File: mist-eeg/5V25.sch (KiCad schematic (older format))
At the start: 14 parts, among them U5 TPS63070

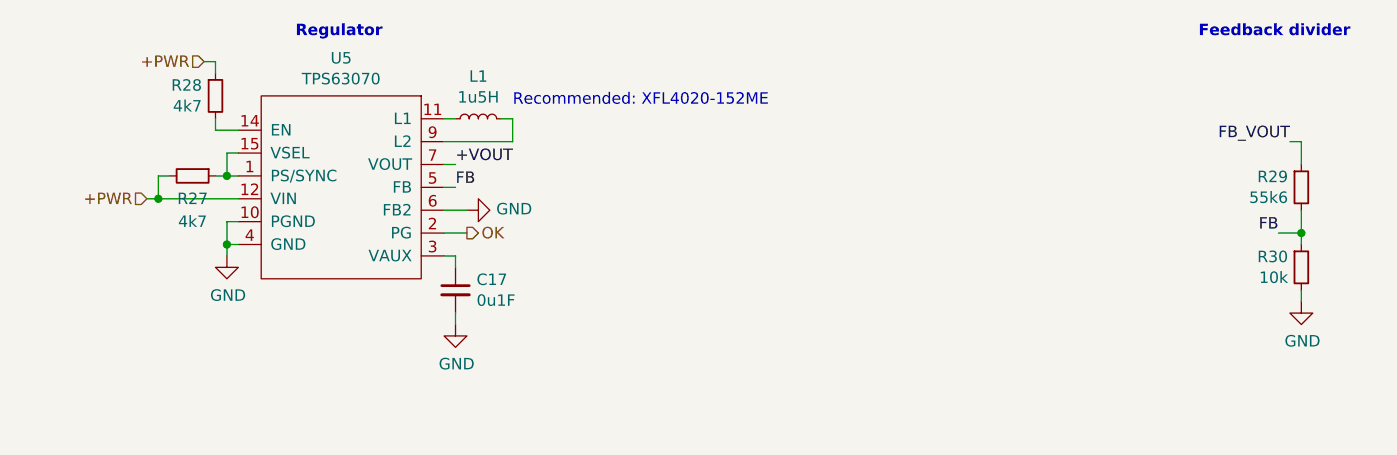
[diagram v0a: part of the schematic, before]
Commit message: Finish schematic and create interface specifications
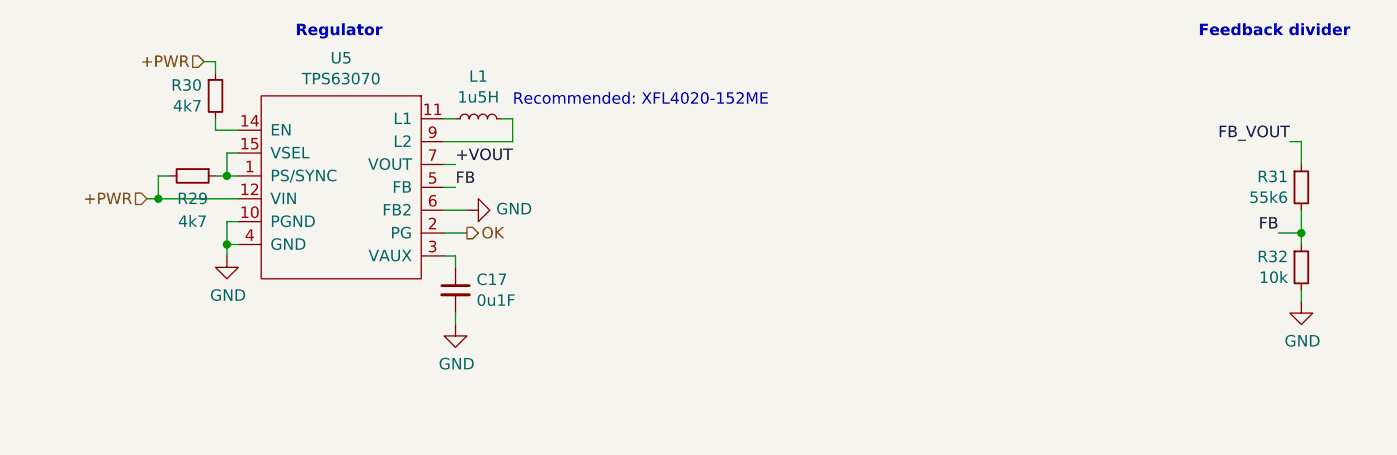
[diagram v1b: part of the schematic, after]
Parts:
- renumbered R27 to R29, R28 to R30, R29 to R31, R30 to R32
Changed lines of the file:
@@
 	3950 2450 4000 2450
 $Comp
-L Device:R_Small R27
+L Device:R_Small R29
 U 1 1 60DC4DE3
 P 3800 2550
-F 0 "R27" V 3900 2550 50  0000 C CNN
+F 0 "R29" V 3900 2550 50  0000 C CNN
 F 1 "4k7" V 4000 2550 50  0000 C CNN
 F 2 "Resistor_SMD:R_0201_0603Metric" H 3800 2550 50  0001 C CNN
@@
 Connection ~ 6250 4500
 $Comp
-L Device:R_Small R29
+L Device:R_Small R31
 U 1 1 60DEB0F2
 P 8650 2600
-F 0 "R29" H 8592 2646 50  0000 R CNN
+F 0 "R31" H 8592 2646 50  0000 R CNN
 F 1 "55k6" H 8592 2555 50  0000 R CNN
 F 2 "Resistor_SMD:R_0603_1608Metric" H 8650 2600 50  0001 C CNN
@@
 $EndComp
 $Comp
-L Device:R_Small R30
+L Device:R_Small R32
 U 1 1 60DEB255
 P 8650 2950
-F 0 "R30" H 8592 2996 50  0000 R CNN
+F 0 "R32" H 8592 2996 50  0000 R CNN
 F 1 "10k" H 8592 2905 50  0000 R CNN
 F 2 "Resistor_SMD:R_0603_1608Metric" H 8650 2950 50  0001 C CNN
@@
 Regulator
 $Comp
-L Device:R_Small R28
+L Device:R_Small R30
 U 1 1 60EEA7D5
 P 3900 2200
-F 0 "R28" H 3841 2246 50  0000 R CNN
+F 0 "R30" H 3841 2246 50  0000 R CNN
 F 1 "4k7" H 3841 2155 50  0000 R CNN
 F 2 "Resistor_SMD:R_0201_0603Metric" H 3900 2200 50  0001 C CNN
@@
 Recommended: XFL4020-152ME
 $Comp
-L power:GND #PWR035
+L power:GND #PWR036
 U 1 1 610AC588
 P 2450 4950
-F 0 "#PWR035" H 2450 4700 50  0001 C CNN
+F 0 "#PWR036" H 2450 4700 50  0001 C CNN
 F 1 "GND" V 2455 4822 50  0000 R CNN
 F 2 "" H 2450 4950 50  0001 C CNN
@@
 $EndComp
 $Comp
-L power:GND #PWR039
+L power:GND #PWR040
 U 1 1 610AC95F
 P 6250 5050
-F 0 "#PWR039" H 6250 4800 50  0001 C CNN
+F 0 "#PWR040" H 6250 4800 50  0001 C CNN
 F 1 "GND" H 6255 4877 50  0000 C CNN
 F 2 "" H 6250 5050 50  0001 C CNN
@@
 $EndComp
 $Comp
-L power:GND #PWR036
+L power:GND #PWR037
 U 1 1 610ACD33
 P 3950 2900
-F 0 "#PWR036" H 3950 2650 50  0001 C CNN
+F 0 "#PWR037" H 3950 2650 50  0001 C CNN
 F 1 "GND" H 3955 2727 50  0000 C CNN
 F 2 "" H 3950 2900 50  0001 C CNN
@@
 $EndComp
 $Comp
-L power:GND #PWR037
+L power:GND #PWR038
 U 1 1 610AD0E9
 P 4950 3200
-F 0 "#PWR037" H 4950 2950 50  0001 C CNN
+F 0 "#PWR038" H 4950 2950 50  0001 C CNN
 F 1 "GND" H 4955 3027 50  0000 C CNN
 F 2 "" H 4950 3200 50  0001 C CNN
@@
 $EndComp
 $Comp
-L power:GND #PWR038
+L power:GND #PWR039
 U 1 1 610AD47F
 P 5000 2700
-F 0 "#PWR038" H 5000 2450 50  0001 C CNN
+F 0 "#PWR039" H 5000 2450 50  0001 C CNN
 F 1 "GND" V 5005 2572 50  0000 R CNN
 F 2 "" H 5000 2700 50  0001 C CNN
@@
 $EndComp
 $Comp
-L power:GND #PWR040
+L power:GND #PWR041
 U 1 1 610AD93A
 P 8650 3100
-F 0 "#PWR040" H 8650 2850 50  0001 C CNN
+F 0 "#PWR041" H 8650 2850 50  0001 C CNN
 F 1 "GND" H 8655 2927 50  0000 C CNN
 F 2 "" H 8650 3100 50  0001 C CNN

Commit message: Validation & fabrication layer
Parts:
- removed R30: 4k7, Resistor_SMD:R_0201_0603Metric, symbol Device:R_Small
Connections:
- net ENA: now reaches U5.14 (EN)
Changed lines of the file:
@@
 Regulator
-$Comp
-L Device:R_Small R30
-U 1 1 60EEA7D5
-P 3900 2200
-F 0 "R30" H 3841 2246 50  0000 R CNN
-F 1 "4k7" H 3841 2155 50  0000 R CNN
-F 2 "Resistor_SMD:R_0201_0603Metric" H 3900 2200 50  0001 C CNN
-F 3 "~" H 3900 2200 50  0001 C CNN
-	1    3900 2200
-	1    0    0    -1
-$EndComp
-Wire Wire Line
-	3900 2300 3900 2350
-Wire Wire Line
-	3900 2350 4000 2350
-Text HLabel 3850 2050 0    50   Input ~ 0
-+PWR
-Wire Wire Line
-	3850 2050 3900 2050
-Wire Wire Line
-	3900 2050 3900 2100
 $Comp
 L Device:C_Small C19
@@
 	1    0    0    -1
 $EndComp
+Text HLabel 3950 2350 0    50   Input ~ 0
+ENA
+Wire Wire Line
+	3950 2350 4000 2350
 $EndSCHEMATC

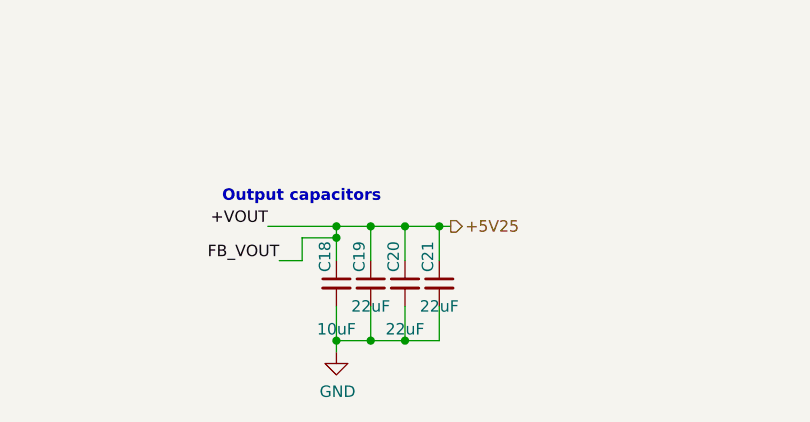
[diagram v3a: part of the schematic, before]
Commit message: Update footprints based upon piece availability & generate manufacturing files
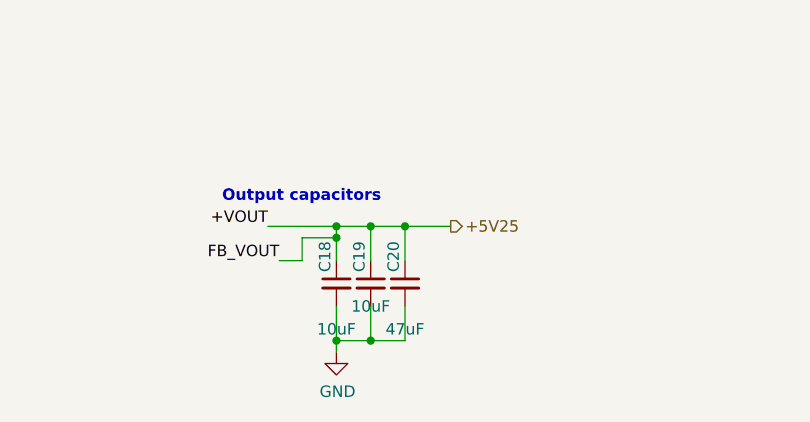
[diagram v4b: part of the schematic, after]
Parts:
- removed C21: 22uF, Capacitor_SMD:C_0603_1608Metric, symbol Device:C_Small
- C19: value 22uF -> 10uF
- C20: value 22uF -> 47uF; footprint Capacitor_SMD:C_0603_1608Metric -> Capacitor_SMD:C_1210_3225Metric
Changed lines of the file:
@@
 P 6400 4750
 F 0 "C19" V 6350 4800 50  0000 L CNN
-F 1 "22uF" H 6400 4650 50  0000 C CNN
+F 1 "10uF" H 6400 4650 50  0000 C CNN
 F 2 "Capacitor_SMD:C_0603_1608Metric" H 6400 4750 50  0001 C CNN
 F 3 "~" H 6400 4750 50  0001 C CNN
@@
 Wire Wire Line
 	6550 4500 6550 4650
-Wire Wire Line
-	6700 4500 6550 4500
-Wire Wire Line
-	6700 4500 6750 4500
-Connection ~ 6700 4500
-Wire Wire Line
-	6700 4500 6700 4650
-$Comp
-L Device:C_Small C21
-U 1 1 60DE3969
-P 6700 4750
-F 0 "C21" V 6650 4800 50  0000 L CNN
-F 1 "22uF" H 6700 4650 50  0000 C CNN
-F 2 "Capacitor_SMD:C_0603_1608Metric" H 6700 4750 50  0001 C CNN
-F 3 "~" H 6700 4750 50  0001 C CNN
-	1    6700 4750
-	1    0    0    -1
-$EndComp
 $Comp
 L Device:C_Small C20
@@
 P 6550 4750
 F 0 "C20" V 6500 4800 50  0000 L CNN
-F 1 "22uF" H 6550 4550 50  0000 C CNN
-F 2 "Capacitor_SMD:C_0603_1608Metric" H 6550 4750 50  0001 C CNN
+F 1 "47uF" H 6550 4550 50  0000 C CNN
+F 2 "Capacitor_SMD:C_1210_3225Metric" H 6550 4750 50  0001 C CNN
 F 3 "~" H 6550 4750 50  0001 C CNN
 	1    6550 4750
@@
 $EndComp
 Wire Wire Line
-	6700 4850 6700 5000
-Wire Wire Line
 	6550 4850 6550 5000
-Wire Wire Line
-	6550 5000 6700 5000
-Connection ~ 6550 5000
 Connection ~ 6400 5000
 Wire Wire Line
@@
 Wire Wire Line
 	3950 2350 4000 2350
+Wire Wire Line
+	6550 4500 6750 4500
 $EndSCHEMATC

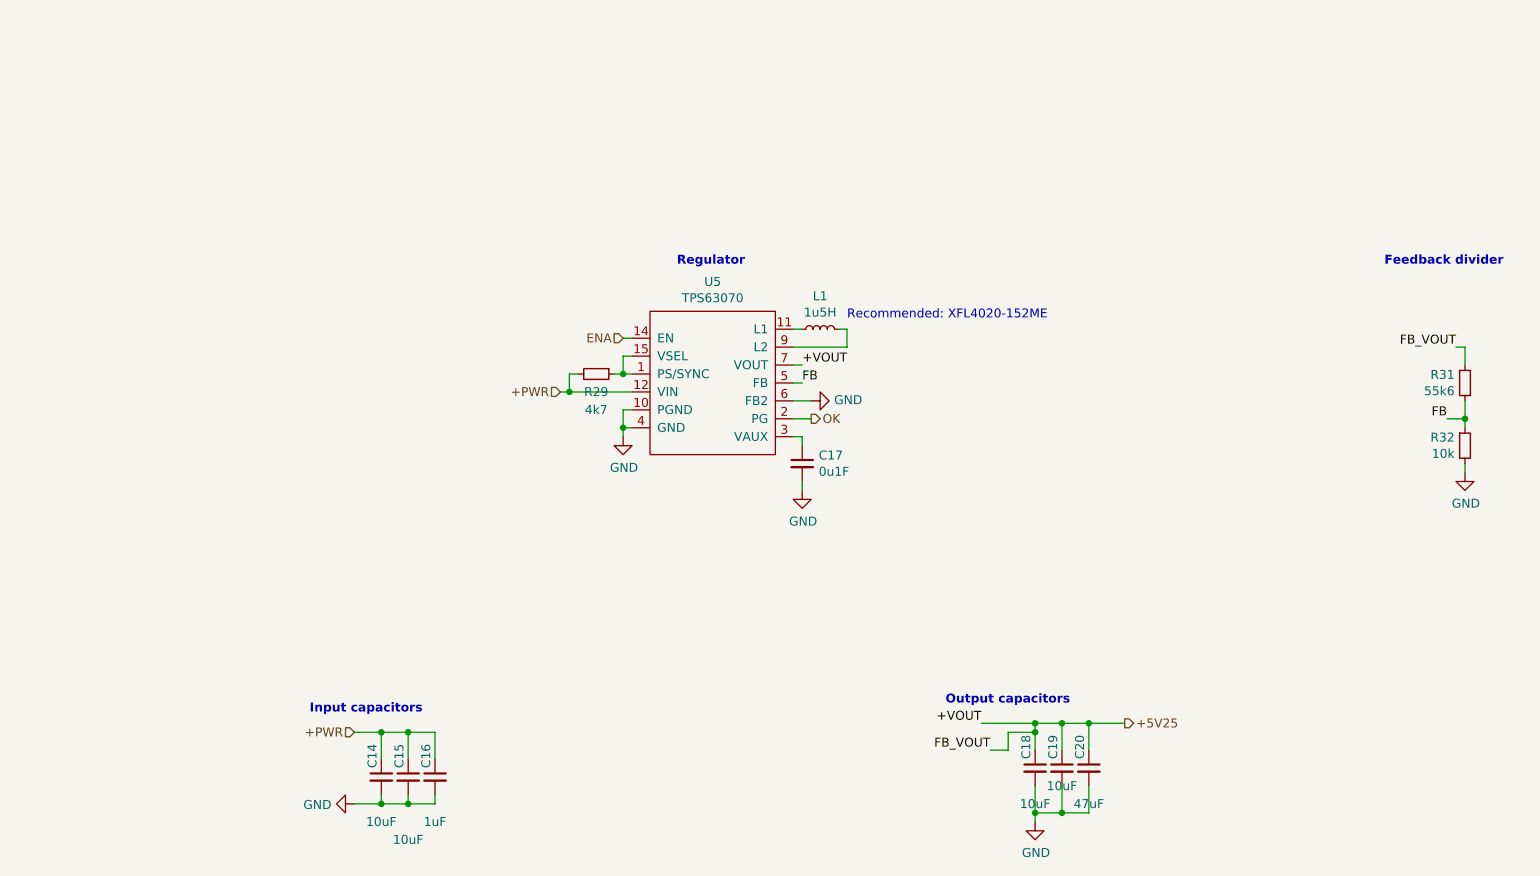
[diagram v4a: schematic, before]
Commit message: Change buckboost regulator used
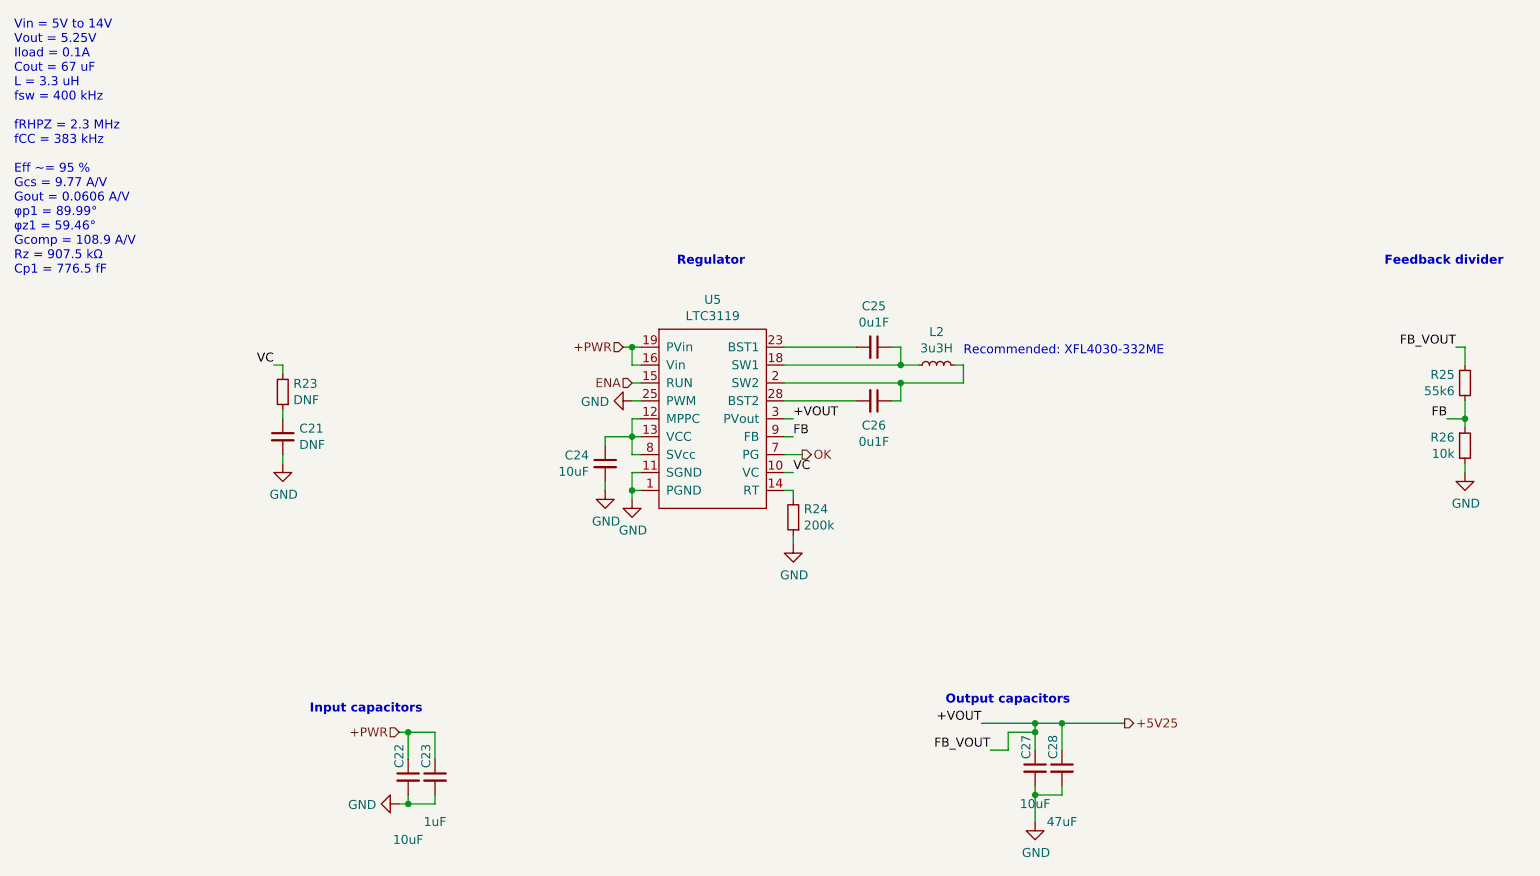
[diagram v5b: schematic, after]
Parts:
- removed C15: 10uF, Capacitor_SMD:C_0603_1608Metric, symbol Device:C_Small
- removed U5: TPS63070, mist-eeg:TPS630702RNMR, symbol components:TPS63070
- added C25, C26: 0u1F, Capacitor_SMD:C_0201_0603Metric, symbol Device:C_Small
- added R23: DNF, Resistor_SMD:R_0201_0603Metric, symbol Device:R_Small
- added U5: LTC3119, Package_DFN_QFN:QFN-28-1EP_4x5mm_P0.5mm_EP2.65x3.65mm, symbol components:LTC3119
- C21: renamed from C17; value 0u1F -> DNF
- L2: renamed from L1; value 1u5H -> 3u3H
- R24: renamed from R29; value 4k7 -> 200k
- renumbered C14 to C22, C16 to C23, C19 to C24, C18 to C27, C20 to C28, R31 to R25, R32 to R26
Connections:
- net +5V25: now also U5.3 (PVout), U5.4 (PVout); no longer C24.1
- net +PWR: now also U5.16 (Vin), U5.19 (PVin), U5.20 (PVin); no longer R24.2
- net ENA: now also U5.15 (RUN)
- net FB: now also U5.9 (FB)
- net GND: now also R24.1, U5.1 (PGND), U5.11 (SGND), U5.17 (PGND), U5.22 (PGND), U5.25 (PWM), U5.29 (PGND), U5.6 (PGND)
- net OK: now also U5.7 (PG)
- net at L2.1: now also C25.1, U5.18 (SW1), U5.21 (SW1)
- net at C21.1: now also R23.1
- net at L2.2: now also C26.1, U5.2 (SW2), U5.5 (SW2)
- new net: R24.2, U5.14 (RT)
- new net: C24.1, U5.12 (MPPC), U5.13 (VCC), U5.8 (SVcc)
- new net: C25.2, U5.23 (BST1)
- new net: C26.2, U5.28 (BST2)
- new net VC: R23.2, U5.10 (VC)
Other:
- note added: "Recommended: XFL4030-332ME"
- note added: "Vin = 5V to 14V\nVout = 5.25V\nIload = 0.1A\nCout = 67 uF\nL = 3.3 uH\nfsw = 400 kHz\n\nfRHPZ = 2.3 MHz\nfCC = 383 kHz\n\nEff ~~= 95 %\nGcs = 9.77 A/V\nGout = 0.0606 A/V\nφp1 = 89.99°\nφz1 = 59.46°\nGcomp = 108.9 A/V\nRz = 907.5 kΩ\nCp1 = 776.5 fF"
- note removed: "Recommended: XFL4020-152ME"
- moved on the sheet: C21, C22, C24, C28, L2, R24
